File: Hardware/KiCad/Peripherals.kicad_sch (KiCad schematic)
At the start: 35 parts

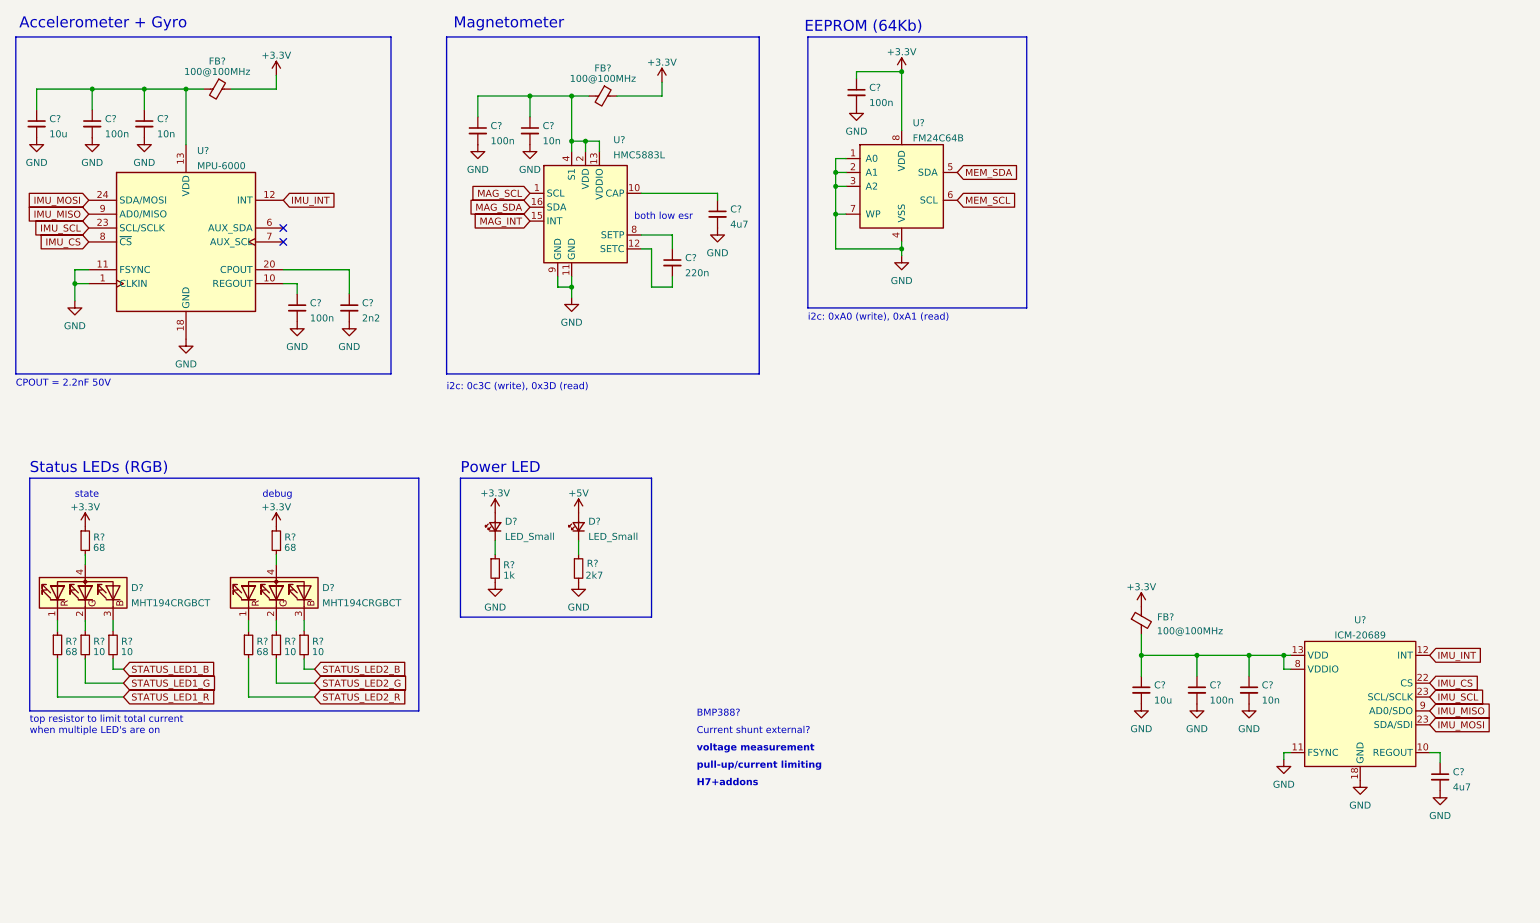
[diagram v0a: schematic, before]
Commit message: added the bmp388 pressure sensor
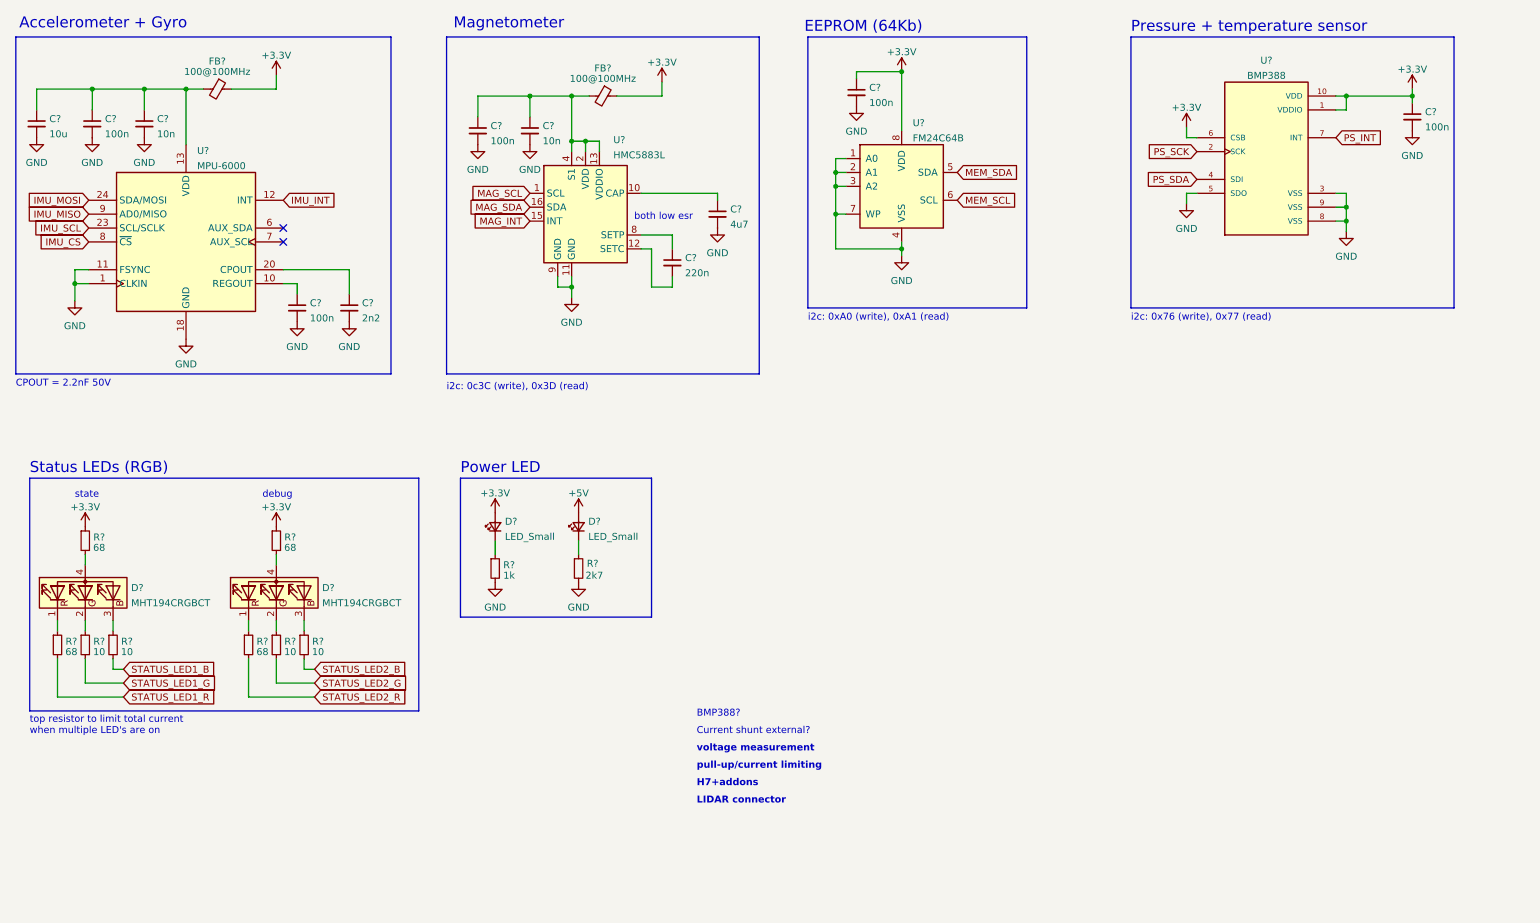
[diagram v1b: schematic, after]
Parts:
- removed C?: 10n, symbol Device:C_Small
- removed C?: 10u, symbol Device:C_Small
- removed C?: 100n, symbol Device:C_Small
- removed C?: 4u7, symbol Device:C_Small
- removed FB?: 100@100MHz, symbol Device:FerriteBead_Small
- removed U?: ICM-20689, Sensor_Motion:InvenSense_QFN-24_4x4mm_P0.5mm, symbol flightController:ICM-20689
- added C?: 100n, symbol Device:C_Small
- added U?: BMP388, PQFN50P200X200X80-10N, symbol flightController:BMP388
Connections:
- net +3V3: now also C?.1, U?.1 (VDDIO), U?.10 (VDD), U?.6 (CSB)
- net GND: now also C?.2, U?.3 (VSS), U?.5 (SDO), U?.8 (VSS), U?.9 (VSS)
- new net PS_INT: U?.7 (INT)
- new net PS_SCK: U?.2 (SCK)
- new net PS_SDA: U?.4 (SDI)
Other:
- note added: "LIDAR connector"
- note added: "Pressure + temperature sensor"
- note added: "i2c: 0x76 (write), 0x77 (read)"

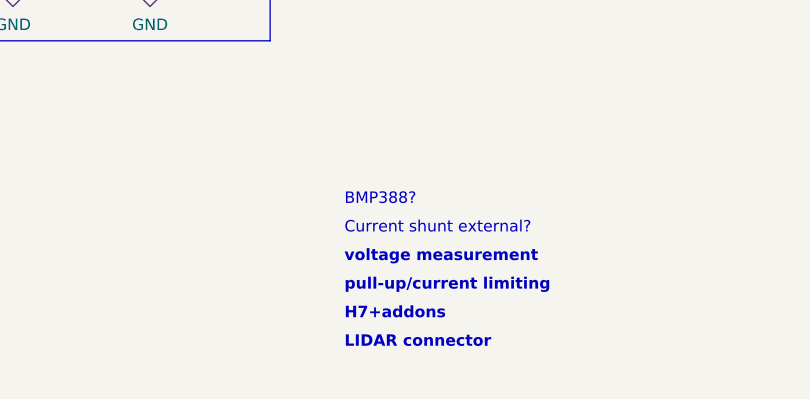
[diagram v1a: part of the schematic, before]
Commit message: changed MCU to STM32H743VIT6
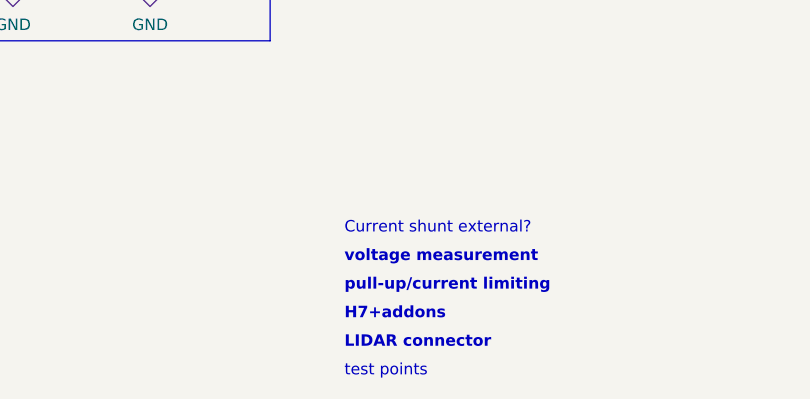
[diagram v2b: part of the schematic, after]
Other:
- note added: "test points"
- note removed: "BMP388?"
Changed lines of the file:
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@@
     (effects (font (size 1.27 1.27) (thickness 0.254) bold) (justify left bottom))
-  )
-  (text "BMP388?" (at 137.795 142.875 0)
-    (effects (font (size 1.27 1.27)) (justify left bottom))
   )
   (text "top resistor to limit total current \nwhen multiple LED's are on"
@@
     (effects (font (size 2 2)) (justify left bottom))
   )
+  (text "test points" (at 137.795 161.925 0)
+    (effects (font (size 1.27 1.27)) (justify left bottom))
+  )
   (text "LIDAR connector" (at 137.795 158.75 0)

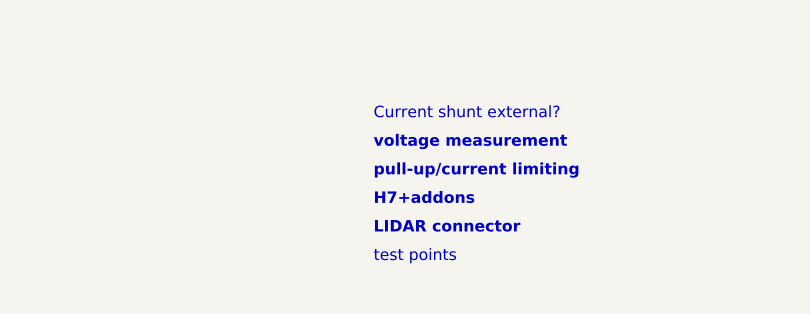
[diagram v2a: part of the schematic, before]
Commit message: Added some pin definitions and drivers for mcu communication
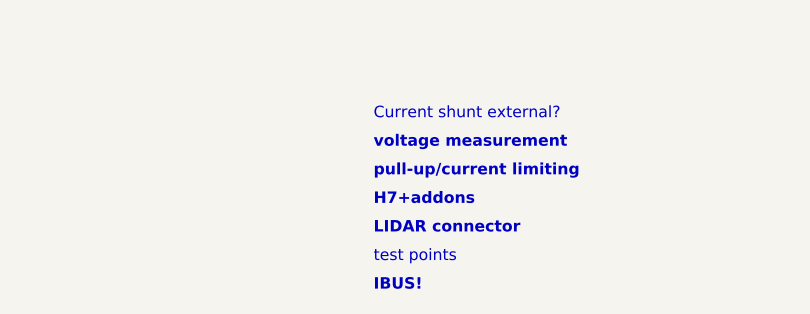
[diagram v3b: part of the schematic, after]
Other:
- note added: "IBUS!"
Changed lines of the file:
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@@
     (effects (font (size 2 2)) (justify left bottom))
+  )
+  (text "IBUS!" (at 137.795 165.1 0)
+    (effects (font (size 1.27 1.27) (thickness 0.254) bold) (justify left bottom))
   )
   (text "i2c: 0x76 (write), 0x77 (read)" (at 217.17 70.485 0)

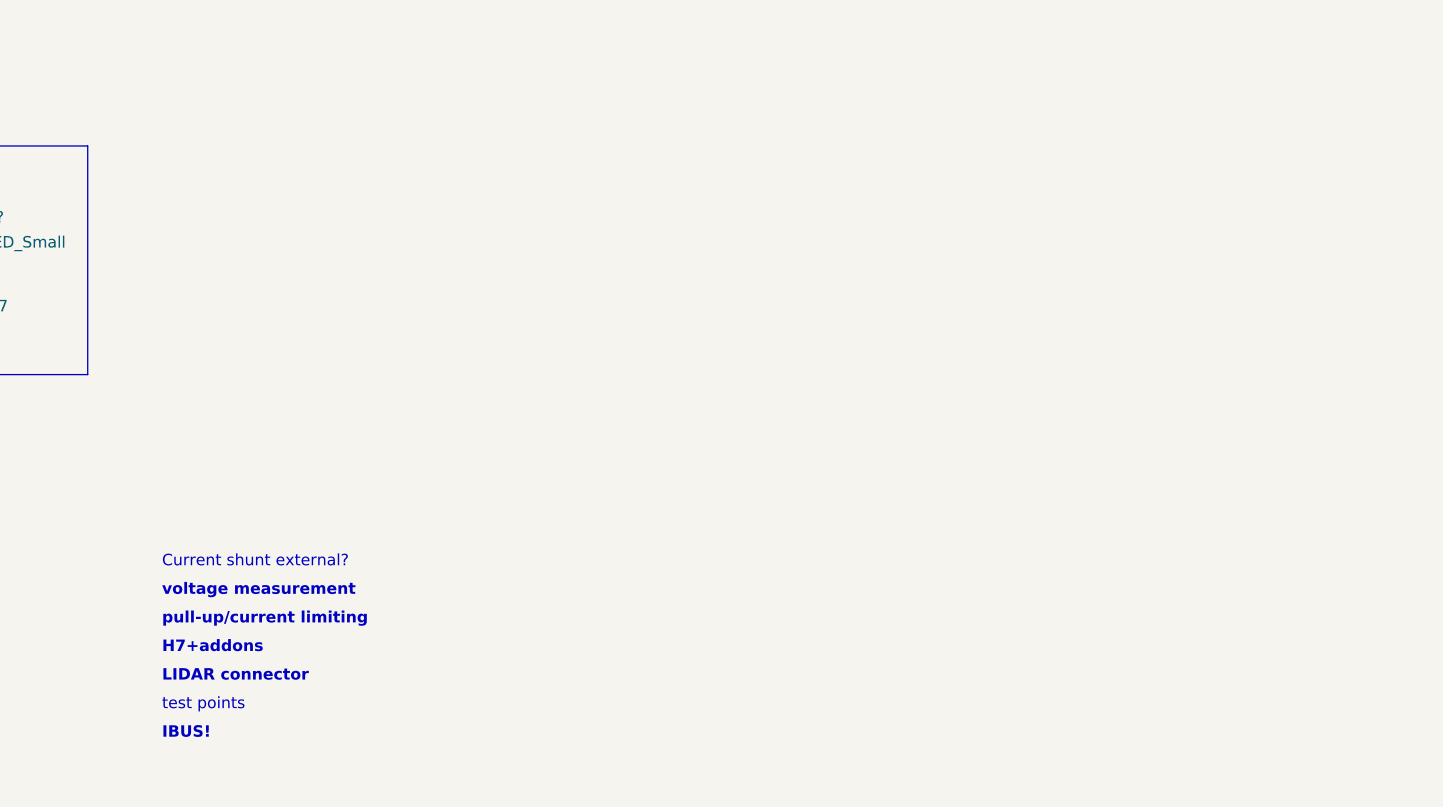
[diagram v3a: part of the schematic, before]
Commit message: Changed max PPM ESC controlers from 8->6 to make room for a buzzer and IBUS connection
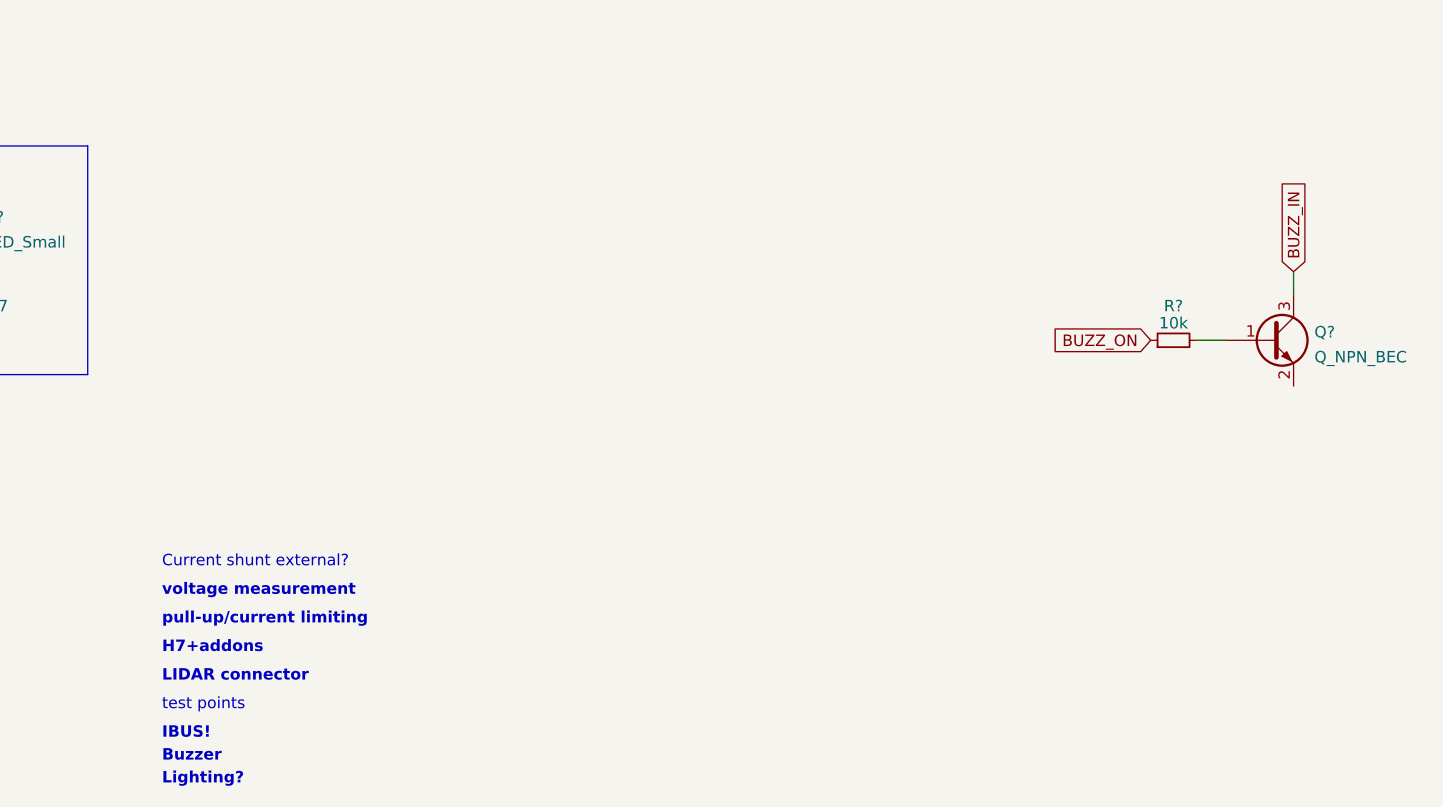
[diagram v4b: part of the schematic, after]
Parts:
- added Q?: Q_NPN_BEC, symbol Device:Q_NPN_BEC
- added R?: 10k, symbol Device:R_Small
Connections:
- new net: Q?.1 (B), R?.2
- new net BUZZ_IN: Q?.3 (C)
- new net BUZZ_ON: R?.1
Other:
- note added: "Buzzer"
- note added: "Lighting?"
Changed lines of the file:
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@@
+    (stroke (width 0) (type default) (color 0 0 0 0))
+  )
+  (wire (pts (xy 263.525 113.03) (xy 263.525 115.57))
     (stroke (width 0) (type default) (color 0 0 0 0))
   )
@@
   )
   (wire (pts (xy 131.445 29.21) (xy 123.19 29.21))
+    (stroke (width 0) (type default) (color 0 0 0 0))
+  )
+  (wire (pts (xy 252.73 120.65) (xy 255.905 120.65))
     (stroke (width 0) (type default) (color 0 0 0 0))
   )
@@
   )
   (text "voltage measurement" (at 137.795 149.225 0)
+    (effects (font (size 1.27 1.27) (thickness 0.254) bold) (justify left bottom))
+  )
+  (text "Lighting?" (at 137.795 170.18 0)
     (effects (font (size 1.27 1.27) (thickness 0.254) bold) (justify left bottom))
   )
@@
   (text "Accelerometer + Gyro" (at 13.97 17.145 0)
     (effects (font (size 2 2)) (justify left bottom))
+  )
+  (text "Buzzer" (at 137.795 167.64 0)
+    (effects (font (size 1.27 1.27) (thickness 0.254) bold) (justify left bottom))
   )
   (text "test points" (at 137.795 161.925 0)
@@
     )
   )
+  (global_label "BUZZ_ON" (shape input) (at 247.65 120.65 180) (fields_autoplaced)
+    (effects (font (size 1.27 1.27)) (justify right))
+    (property "Intersheet References" "${INTERSHEET_REFS}" (id 0) (at 236.5888 120.5706 0)
+      (effects (font (size 1.27 1.27)) (justify right) hide)
+    )
+  )
   (global_label "STATUS_LED1_R" (shape input) (at 33.02 139.065 0) (fields_autoplaced)
     (effects (font (size 1.27 1.27)) (justify left))
     (property "Intersheet References" "${INTERSHEET_REFS}" (id 0) (at 50.0683 138.9856 0)
+      (effects (font (size 1.27 1.27)) (justify left) hide)
+    )
+  )
+  (global_label "BUZZ_IN" (shape input) (at 263.525 113.03 90) (fields_autoplaced)
+    (effects (font (size 1.27 1.27)) (justify left))
+    (property "Intersheet References" "${INTERSHEET_REFS}" (id 0) (at 263.4456 102.6945 90)
       (effects (font (size 1.27 1.27)) (justify left) hide)
     )
@@
     (pin "1")
   )
+  (symbol (lib_id "Device:R_Small") (at 250.19 120.65 90) (unit 1)
+    (in_bom yes) (on_board yes)
+    (property "Reference" "R?" (id 0) (at 250.19 116.84 90))
+    (property "Value" "10k" (id 1) (at 250.19 118.745 90))
+    (property "Footprint" "" (id 2) (at 250.19 120.65 0)
+      (effects (font (size 1.27 1.27)) hide)
+    )
+    (property "Datasheet" "~" (id 3) (at 250.19 120.65 0)
+      (effects (font (size 1.27 1.27)) hide)
+    )
+    (pin "1")
+    (pin "2")
+  )
   (symbol (lib_id "power:GND") (at 27.305 36.83 0) (unit 1)
     (in_bom yes) (on_board yes)
@@
     (pin "1")
   )
+  (symbol (lib_id "Device:Q_NPN_BEC") (at 260.985 120.65 0) (unit 1)
+    (in_bom yes) (on_board yes) (fields_autoplaced)
+    (property "Reference" "Q?" (id 0) (at 265.8364 119.7415 0)
+      (effects (font (size 1.27 1.27)) (justify left))
+    )
+    (property "Value" "Q_NPN_BEC" (id 1) (at 265.8364 122.5166 0)
+      (effects (font (size 1.27 1.27)) (justify left))
+    )
+    (property "Footprint" "" (id 2) (at 266.065 118.11 0)
+      (effects (font (size 1.27 1.27)) hide)
+    )
+    (property "Datasheet" "~" (id 3) (at 260.985 120.65 0)
+      (effects (font (size 1.27 1.27)) hide)
+    )
+    (pin "1")
+    (pin "2")
+    (pin "3")
+  )
   (symbol (lib_id "Device:LED_Small") (at 100.965 107.95 90) (unit 1)
